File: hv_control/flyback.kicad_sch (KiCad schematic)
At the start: 33 parts, among them Q1 TCLT1003, U30 FSL4110LR, U31 ${SIM.PARAMS}

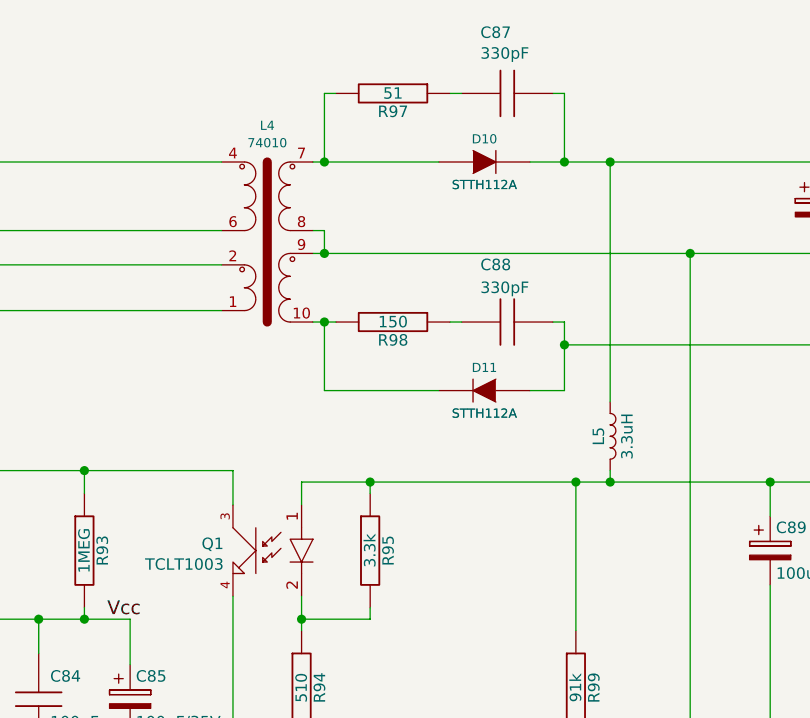
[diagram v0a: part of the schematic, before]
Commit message: lathe.ini for simulation mode.
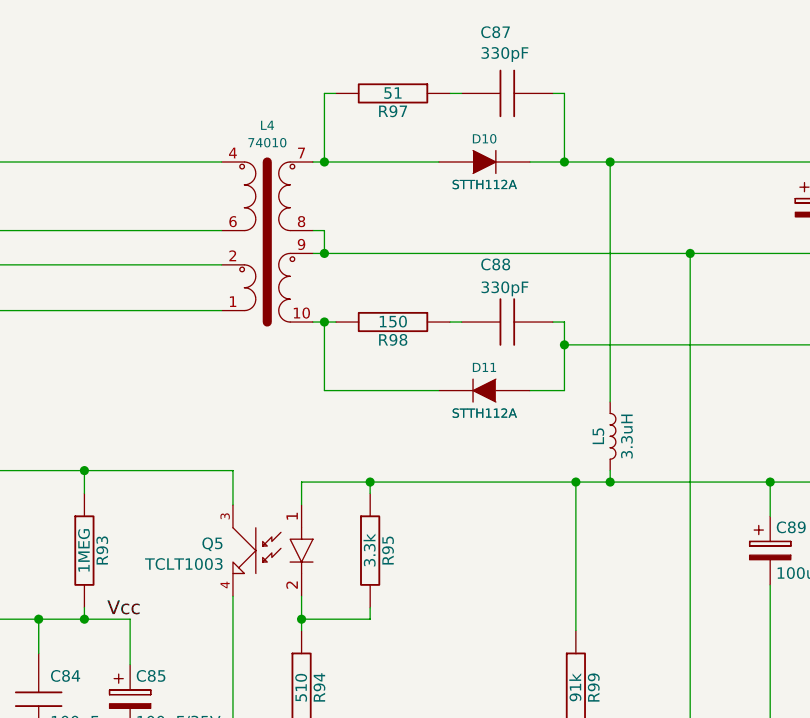
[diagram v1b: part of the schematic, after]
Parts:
- renumbered Q1 to Q5
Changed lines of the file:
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@@
 (kicad_sch
-	(version 20231120)
+	(version 20250114)
 	(generator "eeschema")
-	(generator_version "8.0")
+	(generator_version "9.0")
 	(paper "A4")
+	(text "Double isolation"
+		(exclude_from_sim no)
+		(at 154.94 27.94 0)
+		(effects
+			(font
+				(size 1.524 1.524)
+			)
+			(justify left bottom)
+		)
+	)
+	(text "Add resistor >700V"
+		(exclude_from_sim no)
+		(at 87.63 69.85 90)
+		(effects
+			(font
+				(size 1.27 1.27)
+			)
+			(justify left bottom)
+		)
+	)
+	(text "4.7k -> 6.2k for Cree FETS"
+		(exclude_from_sim no)
+		(at 181.61 148.59 0)
+		(effects
+			(font
+				(size 1.524 1.524)
+			)
+			(justify left bottom)
+		)
+	)
+	(text "Optional"
+		(exclude_from_sim no)
+		(at 72.39 63.5 90)
+		(effects
+			(font
+				(size 1.27 1.27)
+			)
+			(justify left bottom)
+		)
+	)
 	(junction
 		(at 104.14 81.28)
@@
 		)
 	)
-	(text "Double isolation"
-		(exclude_from_sim no)
-		(at 154.94 27.94 0)
-		(effects
-			(font
-				(size 1.524 1.524)
-			)
-			(justify left bottom)
-		)
-	)
-	(text "Add resistor >700V"
-		(exclude_from_sim no)
-		(at 87.63 69.85 90)
-		(effects
-			(font
-				(size 1.27 1.27)
-			)
-			(justify left bottom)
-		)
-	)
-	(text "4.7k -> 6.2k for Cree FETS"
-		(exclude_from_sim no)
-		(at 181.61 148.59 0)
-		(effects
-			(font
-				(size 1.524 1.524)
-			)
-			(justify left bottom)
-		)
-	)
-	(text "Optional"
-		(exclude_from_sim no)
-		(at 72.39 63.5 90)
-		(effects
-			(font
-				(size 1.27 1.27)
-			)
-			(justify left bottom)
-		)
-	)
 	(label "Vstr"
 		(at 82.55 81.28 0)
-		(fields_autoplaced yes)
 		(effects
 			(font
@@
 	(label "Vcc"
 		(at 144.78 100.33 0)
-		(fields_autoplaced yes)
 		(effects
 			(font
@@
 	(label "sw"
 		(at 128.27 49.53 0)
-		(fields_autoplaced yes)
 		(effects
 			(font
@@
 		(shape output)
 		(at 242.57 69.85 0)
-		(fields_autoplaced yes)
 		(effects
 			(font
@@
 		(shape output)
 		(at 242.57 143.51 0)
-		(fields_autoplaced yes)
 		(effects
 			(font
@@
 		(shape input)
 		(at 59.69 49.53 180)
-		(fields_autoplaced yes)
 		(effects
 			(font
@@
 		(shape input)
 		(at 59.69 118.11 180)
-		(fields_autoplaced yes)
 		(effects
 			(font
@@
 		(shape input)
 		(at 240.03 125.73 0)
-		(fields_autoplaced yes)
 		(effects
 			(font
@@
 		(shape output)
 		(at 242.57 85.09 0)
-		(fields_autoplaced yes)
 		(effects
 			(font
@@
 		(dnp no)
 		(fields_autoplaced yes)
-		(property "Reference" "Q1"
+		(property "Reference" "Q5"
 			(at 157.7339 91.9491 0)
 			(effects
@@
 					(unit 1)
 				)
-				(path "/3df459ea-848b-4c48-864f-50e7991fb6c3/00000000-0000-0000-0000-000059b142ac/00000000-0000-0000-0000-00005e1b8050"
-					(reference "Q3")
-					(unit 1)
-				)
 				(path "/3df459ea-848b-4c48-864f-50e7991fb6c3/00000000-0000-0000-0000-000059aa5cec/00000000-0000-0000-0000-00005c5da20b"
 					(reference "Q5")
@@
 					(unit 1)
 				)
+				(path "/3df459ea-848b-4c48-864f-50e7991fb6c3/00000000-0000-0000-0000-000059b142ac/00000000-0000-0000-0000-00005e1b8050"
+					(reference "Q3")
+					(unit 1)
+				)
